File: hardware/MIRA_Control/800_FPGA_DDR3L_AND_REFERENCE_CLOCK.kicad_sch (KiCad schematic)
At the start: 72 parts, among them U500 XC7A200T-2FBG484I, U800 MT41K256M16TW-107:P, Y800 SiT9121AI-2B2-33E200.000000

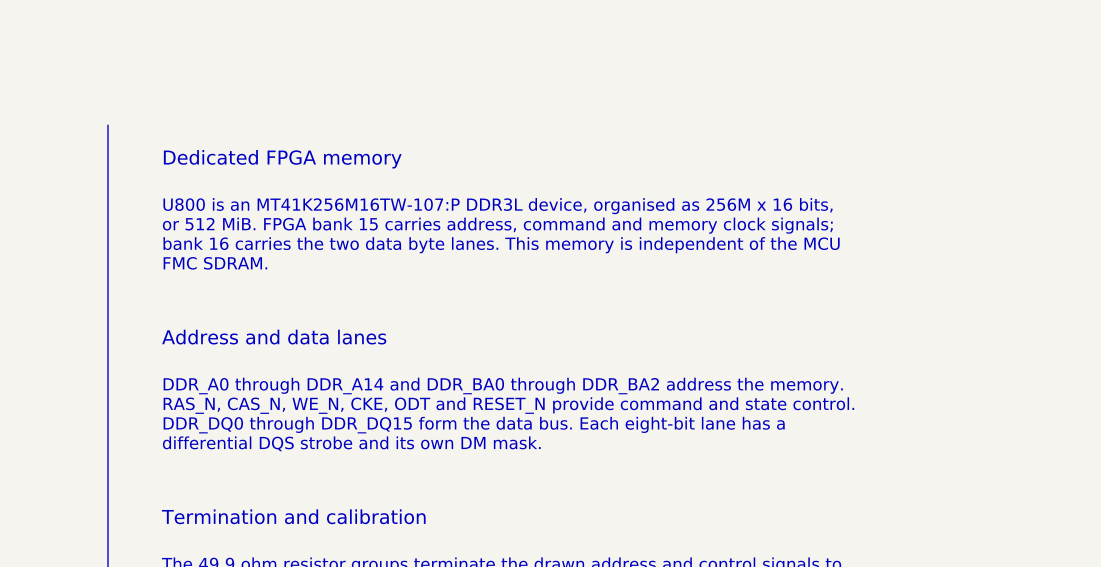
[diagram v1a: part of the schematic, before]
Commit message: Verify digital pin maps and move MCU SPI clock to FPGA SRCC; prepare MIG inputs
MIRA-Digital-Patch: 73ac2f23a7d4a0d4119e0995085469fb50397bb688045691fe4033bcf7fa9ede
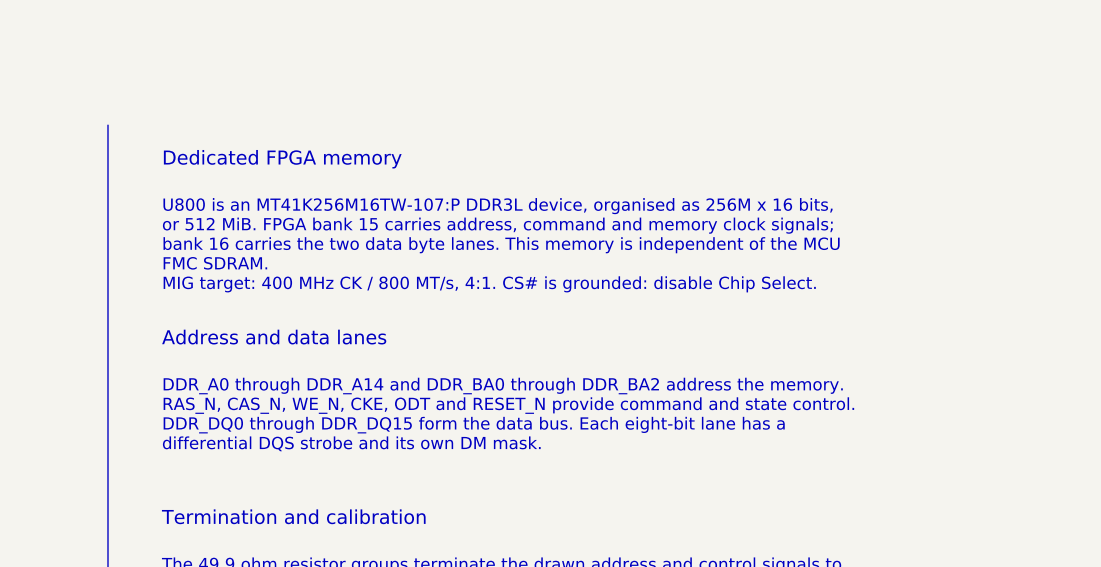
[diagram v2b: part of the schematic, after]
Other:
- note added: "U800 is an MT41K256M16TW-107:P DDR3L device, organised as 256M x 16 bits, or 512 MiB. FPGA bank 15 carries address, command and memory clock signals; bank 16 carries the two data byte lanes. This memory is independent of the MCU FMC SDRAM. MIG target: 400 MHz CK / 800 MT/s, 4:1. CS# is grounded: disable Chip Select."
- note removed: "U800 is an MT41K256M16TW-107:P DDR3L device, organised as 256M x 16 bits, or 512 MiB. FPGA bank 15 carries address, command and memory clock signals; bank 16 carries the two data byte lanes. This memory is independent of the MCU FMC SDRAM."
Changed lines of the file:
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@@
 		)
 	)
-	(text "U800 is an MT41K256M16TW-107:P DDR3L device, organised as 256M x 16 bits,\nor 512 MiB. FPGA bank 15 carries address, command and memory clock signals;\nbank 16 carries the two data byte lanes. This memory is independent of the MCU\nFMC SDRAM."
-		(exclude_from_sim no)
-		(at 315 42.34 0)
-		(effects
-			(font
-				(size 1.35 1.35)
-				(color 0 70 160 1)
-			)
-			(justify left top)
-		)
-	)
+	(text "U800 is an MT41K256M16TW-107:P DDR3L device, organised as 256M x 16 bits,\nor 512 MiB. FPGA bank 15 carries address, command and memory clock signals;\nbank 16 carries the two data byte lanes. This memory is independent of the MCU\nFMC SDRAM.\nMIG target: 400 MHz CK / 800 MT/s, 4:1. CS# is grounded: disable Chip Select." (exclude_from_sim no) (at 315 42.34 0) (effects (font (size 1.35 1.35) (color 0 70 160 1)) (justify left top)))
 	(text "FPGA DDR3L address and command"
 		(exclude_from_sim no)
